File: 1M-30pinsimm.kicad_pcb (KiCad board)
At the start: 4 copper layers, 89 x 16.6 mm, 9 parts, among them U1 JEDEC-FPDRAM, U2 JEDEC-FPDRAM, U3 JEDEC-FPDRAM_Parity

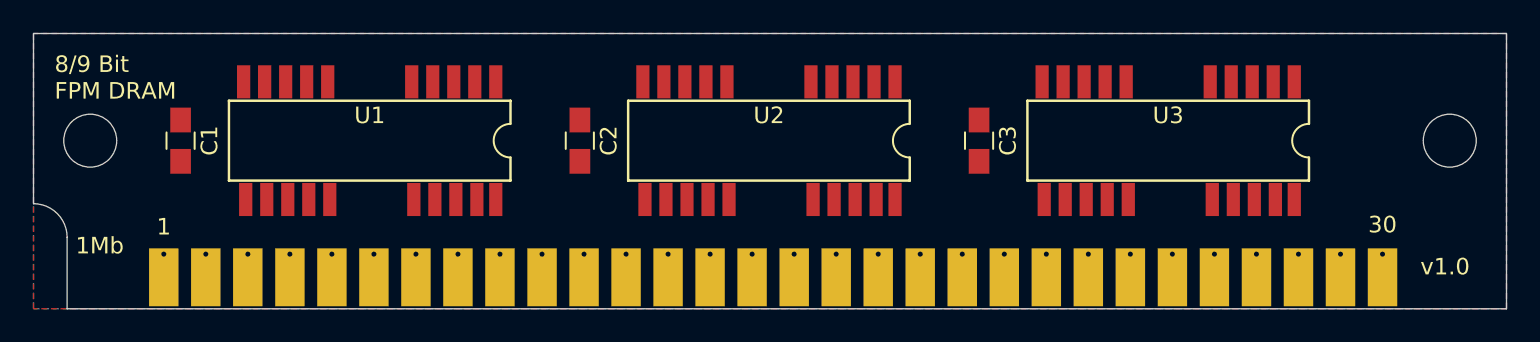
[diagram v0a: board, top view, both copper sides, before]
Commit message: cleaned up tracks
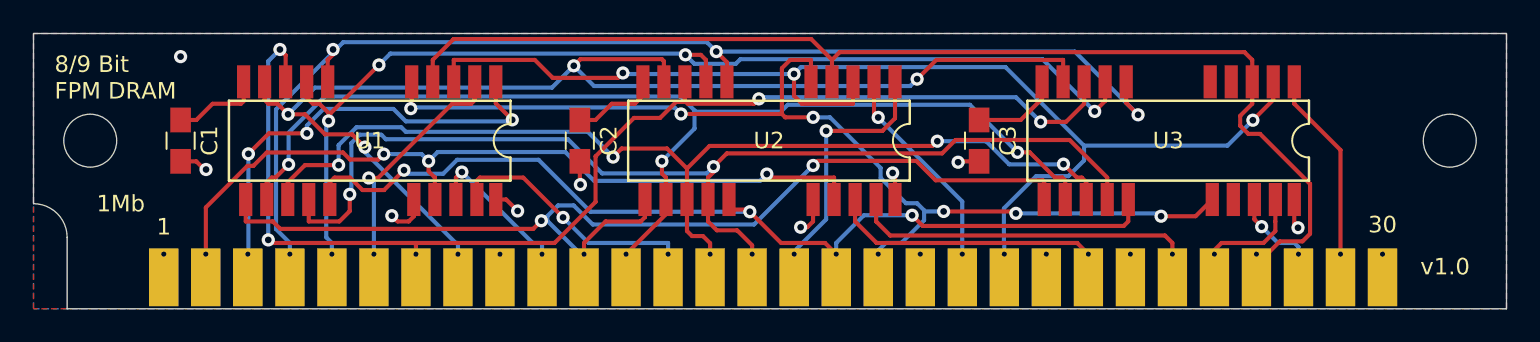
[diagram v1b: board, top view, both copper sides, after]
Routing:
- net A3: track 0.00 -> 74.7 mm, vias 0 -> 4
- net A2: track 0.00 -> 72.9 mm, vias 0 -> 4
- net WE: track 0.00 -> 72.0 mm, vias 0 -> 3
- net A0: track 0.00 -> 71.3 mm, vias 0 -> 3
- net RAS: track 0.00 -> 70.3 mm
- net A5: track 0.00 -> 66.7 mm, vias 0 -> 3
- net A1: track 0.00 -> 65.6 mm, vias 0 -> 4
- net A7: track 0.00 -> 65.4 mm, vias 0 -> 2
- net A9: track 0.00 -> 64.0 mm, vias 0 -> 6
- net A4: track 0.00 -> 63.3 mm, vias 0 -> 2
- net A6: track 0.00 -> 61.8 mm, vias 0 -> 4
- net A8: track 0.00 -> 58.0 mm, vias 0 -> 3
- net CAS: track 0.00 -> 47.7 mm, vias 0 -> 3
- net DQ0: track 0.00 -> 26.5 mm, vias 0 -> 3
- net DQ7: track 0.00 -> 20.4 mm
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
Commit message: Update 1M-30pinsimm.kicad_pcb
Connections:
- C1 pad 1: Net-(C1-Pad1) -> +5V
- C1 pad 2: +5V -> GND
- C2 pad 1: Net-(C2-Pad1) -> +5V
- C2 pad 2: +5V -> GND
- C3 pad 1: Net-(C3-Pad1) -> +5V
- C3 pad 2: +5V -> GND
- U1 pad 13: Net-(C1-Pad1) -> +5V
- U2 pad 13: Net-(C2-Pad1) -> +5V
- U3 pad 13: Net-(C3-Pad1) -> +5V
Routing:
- net +5V: track 4.45 -> 18.7 mm
- net GND: track 9.92 -> 16.0 mm, vias 6 -> 9
- net Net-(C1-Pad1): track 5.45 -> 0.00 mm
- net Net-(C3-Pad1): track 5.36 -> 0.00 mm
- net Net-(C2-Pad1): track 5.26 -> 0.00 mm
